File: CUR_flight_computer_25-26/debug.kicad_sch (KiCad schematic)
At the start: 0 parts

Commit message: added dubugging
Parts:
- added D6, D7: ESDA5V3SC5, Package_TO_SOT_SMD:SOT-23-5, symbol Power_Protection:ESDA5V3SC5
- added J6: 3220-14-0100-00, Connector_CNC_Tech:CNC_Tech_3220-14-0100-00, symbol Connector:Conn_ST_STDC14
- added R39: 150, Resistor_SMD:R_0603_1608Metric, symbol Device:R_Small_US
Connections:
- new net: J6.11 (GNDDetect), R39.1
- new net +3V3: J6.3 (VCC)
- new net GND: D6.2 (A), D7.2 (A), J6.5 (GND), J6.7 (GND), R39.2
- new net JCLK/SWCLK: D6.1 (K), J6.6 (JCLK/SWCLK)
- new net JTDI: D6.5 (K), J6.10 (JTDI/NC)
- new net JTDO/SWO: D6.4 (K), J6.8 (JTDO/SWO)
- new net JTMS/SWDIO: D6.3 (K), J6.4 (JTMS/SWDIO)
- new net VCP_RX: D7.5 (K), J6.13 (VCP_RX)
- new net VCP_TX: D7.1 (K), J6.14 (VCP_TX)
- new net ~{RESET}: D7.3 (K), J6.12 (~{RST})
- no-connect marks 0 -> 2
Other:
- note added: "ESD Protection"
- note added: "Reserved (UM2910 pg 11)"
- note added: "Using STLink to align with airbrakes and not pay $50 for the tag connect"
- note added: "also just 02x07 1.27mm so we can do whatever"
- note added: "for STLINK-V3MINIE"
- note added: "meant to be 100 can replace from SMD sampler book if needed"
- note added: "see UM2910 from the debugger's perspective: T_VCP_RX is output T_VCP_TX is input"

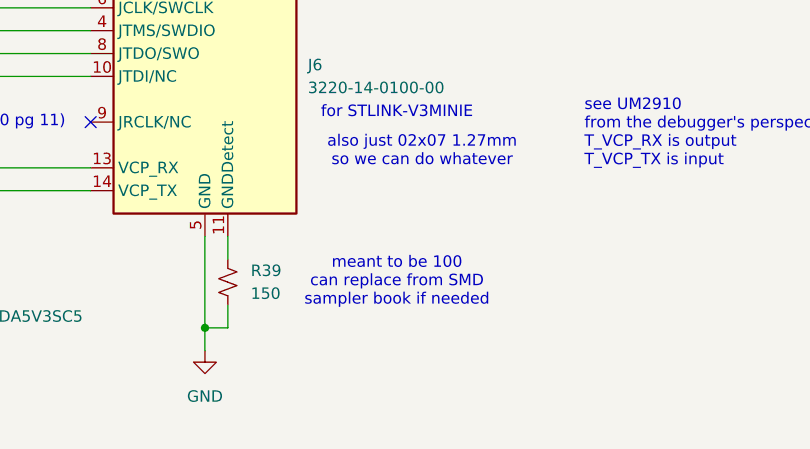
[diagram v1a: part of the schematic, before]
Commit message: changed boot to spdt
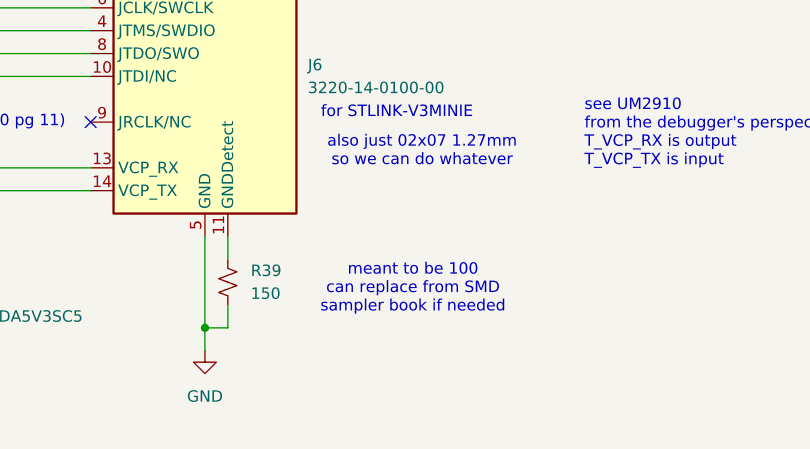
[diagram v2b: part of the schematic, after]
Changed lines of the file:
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@@
 	(text "meant to be 100\ncan replace from SMD\nsampler book if needed"
 		(exclude_from_sim no)
-		(at 134.366 69.85 0)
+		(at 136.144 70.612 0)
 		(effects
 			(font

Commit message: updated all needed fixes
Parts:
- renumbered D6 to D1, D7 to D2, J6 to J1, R39 to R6
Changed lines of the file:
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@@
 		(dnp no)
 		(fields_autoplaced yes)
-		(property "Reference" "J6"
+		(property "Reference" "J1"
 			(at 124.46 45.7199 0)
 			(effects
@@
 			(project "CUR_flight_computer_25-26"
 				(path "/bf7761cc-1b32-4d86-809c-5f027005229b/0389a778-0ae1-4921-8e0e-3c33d2286cb8"
-					(reference "J6")
+					(reference "J1")
 					(unit 1)
 				)
@@
 		(dnp no)
 		(fields_autoplaced yes)
-		(property "Reference" "R39"
+		(property "Reference" "R6"
 			(at 118.11 68.5799 0)
 			(effects
@@
 			(project "CUR_flight_computer_25-26"
 				(path "/bf7761cc-1b32-4d86-809c-5f027005229b/0389a778-0ae1-4921-8e0e-3c33d2286cb8"
-					(reference "R39")
+					(reference "R6")
 					(unit 1)
 				)
@@
 		(dnp no)
 		(fields_autoplaced yes)
-		(property "Reference" "#PWR078"
+		(property "Reference" "#PWR043"
 			(at 113.03 83.82 0)
 			(effects
@@
 			(project "CUR_flight_computer_25-26"
 				(path "/bf7761cc-1b32-4d86-809c-5f027005229b/0389a778-0ae1-4921-8e0e-3c33d2286cb8"
-					(reference "#PWR078")
+					(reference "#PWR043")
 					(unit 1)
 				)
@@
 		(on_board yes)
 		(dnp no)
-		(property "Reference" "D6"
+		(property "Reference" "D1"
 			(at 62.23 71.12 0)
 			(effects
@@
 			(project "CUR_flight_computer_25-26"
 				(path "/bf7761cc-1b32-4d86-809c-5f027005229b/0389a778-0ae1-4921-8e0e-3c33d2286cb8"
-					(reference "D6")
+					(reference "D1")
 					(unit 1)
 				)
@@
 		(dnp no)
 		(fields_autoplaced yes)
-		(property "Reference" "#PWR073"
+		(property "Reference" "#PWR040"
 			(at 54.61 86.36 0)
 			(effects
@@
 			(project "CUR_flight_computer_25-26"
 				(path "/bf7761cc-1b32-4d86-809c-5f027005229b/0389a778-0ae1-4921-8e0e-3c33d2286cb8"
-					(reference "#PWR073")
+					(reference "#PWR040")
 					(unit 1)
 				)
@@
 		(on_board yes)
 		(dnp no)
-		(property "Reference" "D7"
+		(property "Reference" "D2"
 			(at 87.884 71.12 0)
 			(effects
@@
 			(project "CUR_flight_computer_25-26"
 				(path "/bf7761cc-1b32-4d86-809c-5f027005229b/0389a778-0ae1-4921-8e0e-3c33d2286cb8"
-					(reference "D7")
+					(reference "D2")
 					(unit 1)
 				)
@@
 		(dnp no)
 		(fields_autoplaced yes)
-		(property "Reference" "#PWR077"
+		(property "Reference" "#PWR042"
 			(at 113.03 30.48 0)
 			(effects
@@
 			(project "CUR_flight_computer_25-26"
 				(path "/bf7761cc-1b32-4d86-809c-5f027005229b/0389a778-0ae1-4921-8e0e-3c33d2286cb8"
-					(reference "#PWR077")
+					(reference "#PWR042")
 					(unit 1)
 				)
@@
 		(dnp no)
 		(fields_autoplaced yes)
-		(property "Reference" "#PWR074"
+		(property "Reference" "#PWR041"
 			(at 80.01 86.36 0)
 			(effects
@@
 			(project "CUR_flight_computer_25-26"
 				(path "/bf7761cc-1b32-4d86-809c-5f027005229b/0389a778-0ae1-4921-8e0e-3c33d2286cb8"
-					(reference "#PWR074")
-					(unit 1)
-				)
+					(reference "#PWR041")
+					(unit 1)
+				)

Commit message: ahhhh my eyes (decent layout)
put things on both sides
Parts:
- J1: footprint Connector_CNC_Tech:CNC_Tech_3220-14-0100-00 -> Connector_CNC_Tech:CNC_Tech_3020-14-0300-00_CNC
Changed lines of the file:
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@@
 			)
 		)
-		(property "Footprint" "Connector_CNC_Tech:CNC_Tech_3220-14-0100-00"
+		(property "Footprint" "Connector_CNC_Tech:CNC_Tech_3020-14-0300-00_CNC"
 			(at 113.03 46.99 0)
 			(effects

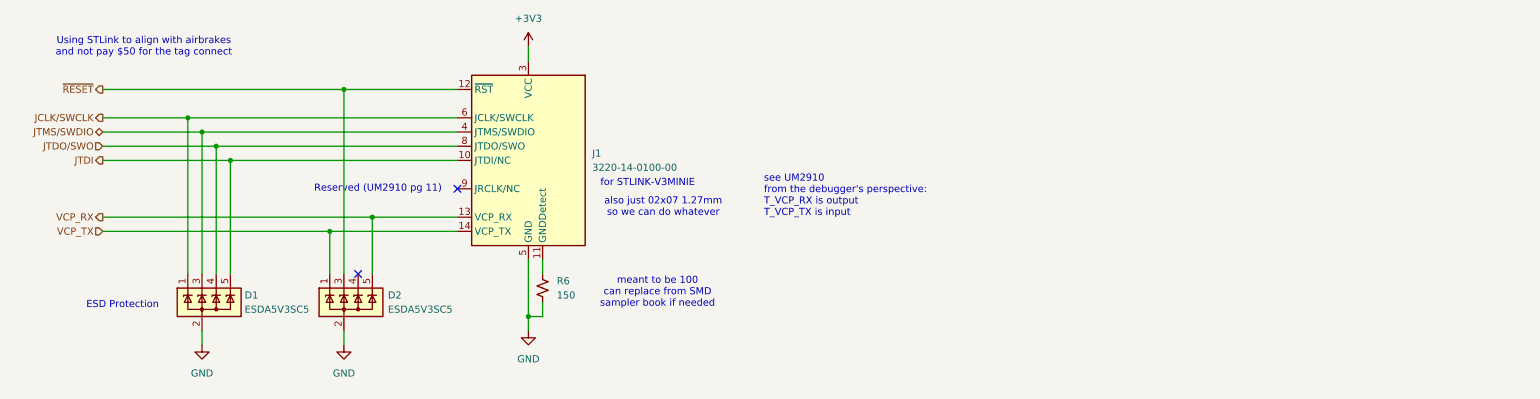
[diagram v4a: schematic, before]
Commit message: added in debug header to layout
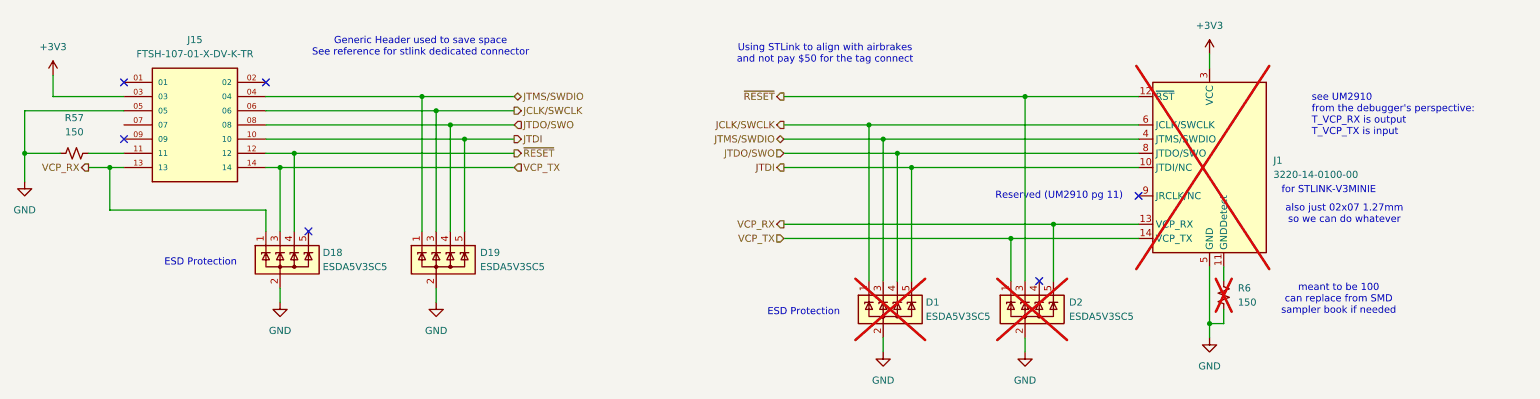
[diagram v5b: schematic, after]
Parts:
- added D18, D19: ESDA5V3SC5, Package_TO_SOT_SMD:SOT-23-5, symbol Power_Protection:ESDA5V3SC5
- added J15: FTSH-107-01-X-DV-K-TR, Connector_SAMTEC_FTSH-107-01-X-DV-K-TR:SAMTEC_FTSH-107-01-X-DV-K-TR, symbol Samtec_FTSH-107-01-X-DV-K-TR:FTSH-107-01-X-DV-K-TR
- added R57: 150, Resistor_SMD:R_0603_1608Metric, symbol Device:R_Small_US
- D1, D2, R6: now not fitted; now left out of the parts list
- J1: footprint Connector_CNC_Tech:CNC_Tech_3020-14-0300-00_CNC -> Connector_SAMTEC_FTSH-107-01-X-DV-K-TR:SAMTEC_FTSH-107-01-X-DV-K-TR; now not fitted; now left out of the parts list
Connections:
- net +3V3: now also J15.03
- net GND: now also D18.2 (A), D19.2 (A), J15.05, R57.1
- net JCLK/SWCLK: now also D19.3 (K), J15.06
- net JTDI: now also D19.5 (K), J15.10
- net JTDO/SWO: now also D19.4 (K), J15.08
- net JTMS/SWDIO: now also D19.1 (K), J15.04
- net VCP_RX: now also D18.1 (K), J15.13
- net VCP_TX: now also D18.3 (K), J15.14
- net ~{RESET}: now also D18.4 (K), J15.12
- new net: J15.11, R57.2
- no-connect marks 2 -> 6
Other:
- note added: "Generic Header used to save space See reference for stlink dedicated connector"

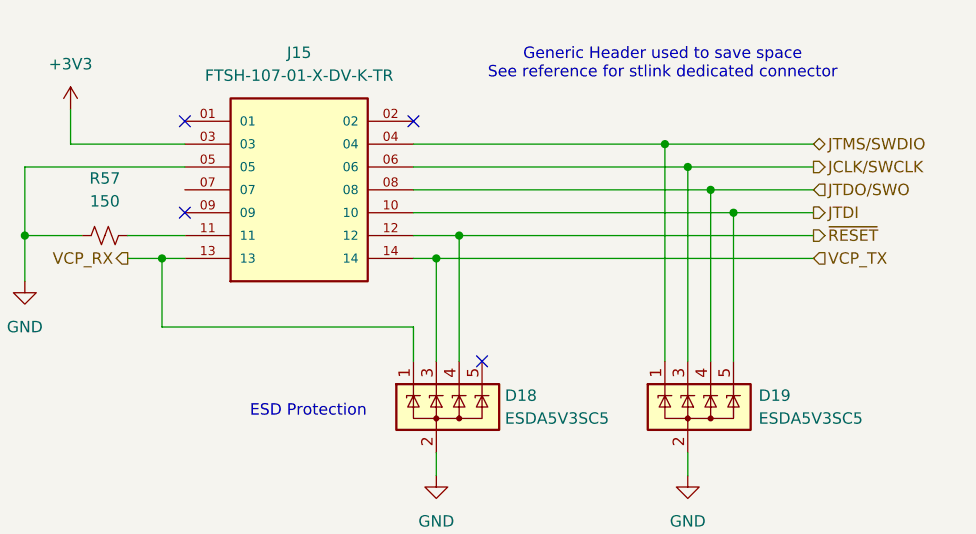
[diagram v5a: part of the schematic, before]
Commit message: started routing power and rf section
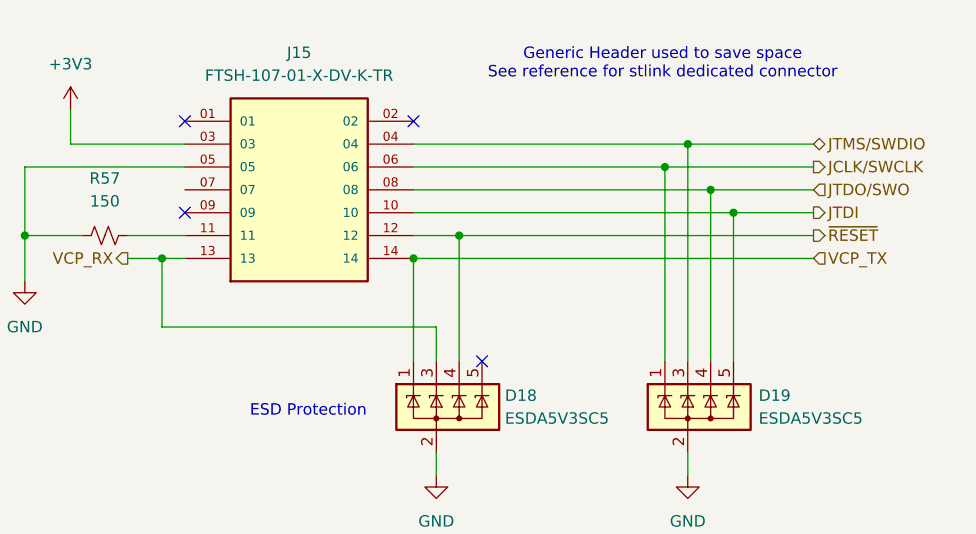
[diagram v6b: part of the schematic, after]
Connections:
- net JCLK/SWCLK: now also D19.1 (K); no longer D19.3 (K)
- net JTMS/SWDIO: now also D19.3 (K); no longer D19.1 (K)
- net VCP_RX: now also D18.3 (K); no longer D18.1 (K)
- net VCP_TX: now also D18.1 (K); no longer D18.3 (K)
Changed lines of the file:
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@@
 	)
 	(junction
-		(at 93.98 35.56)
-		(diameter 0)
-		(color 0 0 0 0)
-	)
-	(junction
-		(at 68.58 48.26)
+		(at 93.98 38.1)
 		(diameter 0)
 		(color 0 0 0 0)
@@
 	)
 	(junction
-		(at 96.52 38.1)
-		(diameter 0)
-		(color 0 0 0 0)
-	)
-	(junction
 		(at 38.1 48.26)
 		(diameter 0)
@@
 	)
 	(junction
+		(at 66.04 48.26)
+		(diameter 0)
+		(color 0 0 0 0)
+	)
+	(junction
 		(at 22.86 45.72)
 		(diameter 0)
@@
 	(junction
 		(at 101.6 43.18)
+		(diameter 0)
+		(color 0 0 0 0)
+	)
+	(junction
+		(at 96.52 35.56)
 		(diameter 0)
 		(color 0 0 0 0)
@@
 	(wire
 		(pts
+			(xy 66.04 35.56) (xy 96.52 35.56)
+		)
+		(stroke
+			(width 0)
+			(type default)
+		)
+	)
+	(wire
+		(pts
+			(xy 66.04 59.69) (xy 66.04 48.26)
+		)
+		(stroke
+			(width 0)
+			(type default)
+		)
+	)
+	(wire
+		(pts
 			(xy 99.06 40.64) (xy 110.49 40.64)
 		)
@@
 	(wire
 		(pts
-			(xy 93.98 35.56) (xy 93.98 59.69)
-		)
-		(stroke
-			(width 0)
-			(type default)
-		)
-	)
-	(wire
-		(pts
 			(xy 66.04 43.18) (xy 101.6 43.18)
 		)
@@
 	(wire
 		(pts
+			(xy 68.58 55.88) (xy 68.58 59.69)
+		)
+		(stroke
+			(width 0)
+			(type default)
+		)
+	)
+	(wire
+		(pts
 			(xy 71.12 45.72) (xy 110.49 45.72)
 		)
@@
 	(wire
 		(pts
-			(xy 96.52 38.1) (xy 110.49 38.1)
+			(xy 93.98 38.1) (xy 110.49 38.1)
+		)
+		(stroke
+			(width 0)
+			(type default)
+		)
+	)
+	(wire
+		(pts
+			(xy 66.04 38.1) (xy 93.98 38.1)
 		)
 		(stroke
@@
 	(wire
 		(pts
-			(xy 66.04 59.69) (xy 66.04 55.88)
-		)
-		(stroke
-			(width 0)
-			(type default)
-		)
-	)
-	(wire
-		(pts
 			(xy 158.75 35.56) (xy 201.93 35.56)
 		)
@@
 	(wire
 		(pts
-			(xy 68.58 48.26) (xy 110.49 48.26)
+			(xy 66.04 48.26) (xy 110.49 48.26)
 		)
 		(stroke
@@
 	(wire
 		(pts
-			(xy 66.04 55.88) (xy 38.1 55.88)
+			(xy 38.1 55.88) (xy 68.58 55.88)
+		)
+		(stroke
+			(width 0)
+			(type default)
+		)
+	)
+	(wire
+		(pts
+			(xy 93.98 38.1) (xy 93.98 59.69)
 		)
 		(stroke
@@
 	(wire
 		(pts
-			(xy 68.58 48.26) (xy 68.58 59.69)
-		)
-		(stroke
-			(width 0)
-			(type default)
-		)
-	)
-	(wire
-		(pts
 			(xy 158.75 43.18) (xy 176.53 43.18)
 		)
@@
 	(wire
 		(pts
+			(xy 96.52 35.56) (xy 110.49 35.56)
+		)
+		(stroke
+			(width 0)
+			(type default)
+		)
+	)
+	(wire
+		(pts
 			(xy 201.93 35.56) (xy 222.25 35.56)
 		)
@@
 	(wire
 		(pts
-			(xy 66.04 38.1) (xy 96.52 38.1)
-		)
-		(stroke
-			(width 0)
-			(type default)
-		)
-	)
-	(wire
-		(pts
 			(xy 101.6 43.18) (xy 101.6 59.69)
 		)
@@
 	(wire
 		(pts
-			(xy 93.98 35.56) (xy 110.49 35.56)
-		)
-		(stroke
-			(width 0)
-			(type default)
-		)
-	)
-	(wire
-		(pts
 			(xy 237.49 68.58) (xy 237.49 66.04)
 		)
@@
 	(wire
 		(pts
-			(xy 96.52 38.1) (xy 96.52 59.69)
-		)
-		(stroke
-			(width 0)
-			(type default)
-		)
-	)
-	(wire
-		(pts
 			(xy 66.04 45.72) (xy 71.12 45.72)
 		)
@@
 	(wire
 		(pts
+			(xy 96.52 35.56) (xy 96.52 59.69)
+		)
+		(stroke
+			(width 0)
+			(type default)
+		)
+	)
+	(wire
+		(pts
 			(xy 27.94 31.75) (xy 27.94 35.56)
 		)
@@
 	(wire
 		(pts
-			(xy 66.04 35.56) (xy 93.98 35.56)
-		)
-		(stroke
-			(width 0)
-			(type default)
-		)
-	)
-	(wire
-		(pts
 			(xy 176.53 78.74) (xy 176.53 81.28)
 		)
@@
 		)
 		(stroke
-			(width 0)
-			(type default)
-		)
-	)
-	(wire
-		(pts
-			(xy 66.04 48.26) (xy 68.58 48.26)
-		)
-		(stroke

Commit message: Layout groups
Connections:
- net JCLK/SWCLK: now also D19.3 (K); no longer D19.1 (K)
- net JTDI: now also D18.5 (K); no longer D19.5 (K)
- net JTMS/SWDIO: now also D19.1 (K); no longer D19.3 (K)
- net VCP_RX: now also D18.4 (K); no longer D18.3 (K)
- net VCP_TX: now also D18.3 (K); no longer D18.1 (K)
- net ~{RESET}: now also D18.1 (K); no longer D18.4 (K)
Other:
- moved on the sheet: D18

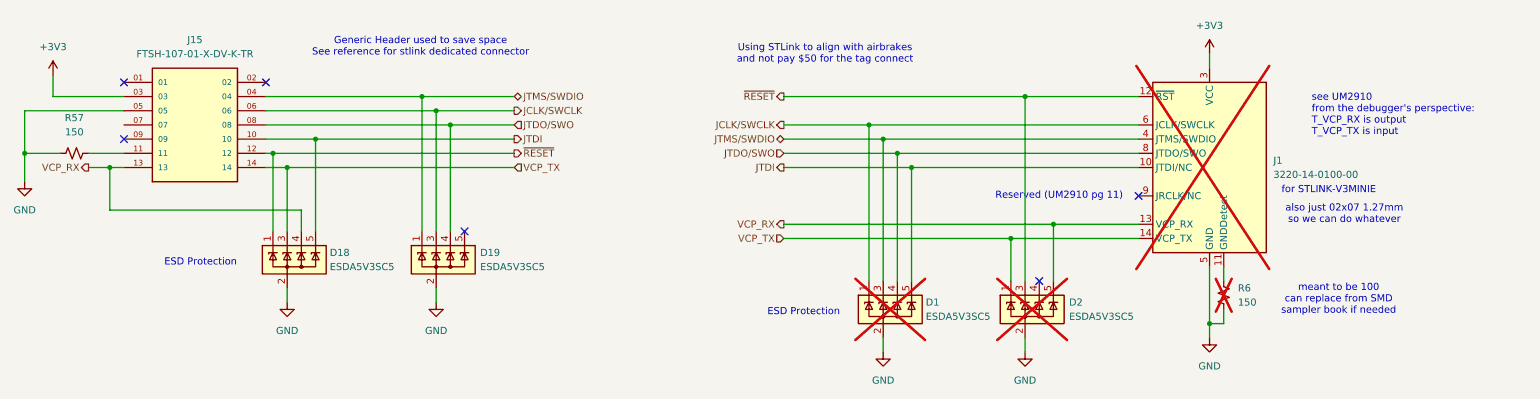
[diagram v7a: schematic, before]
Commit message: Remove JTDI and combine NRST and ~{RESET}
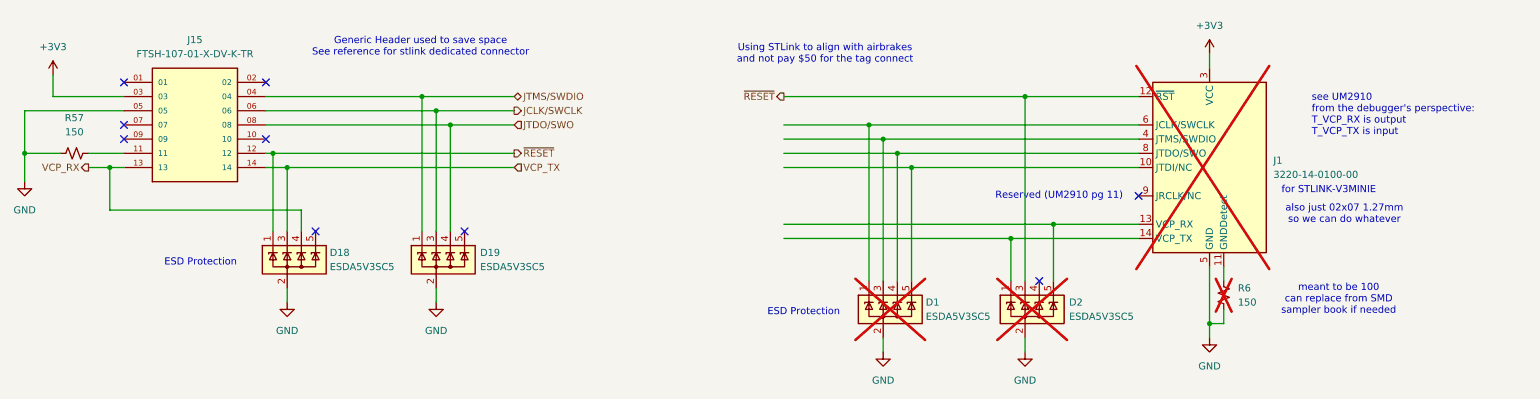
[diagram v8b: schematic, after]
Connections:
- net JCLK/SWCLK: no longer D1.1 (K), J1.6 (JCLK/SWCLK)
- net JTDO/SWO: no longer D1.4 (K), J1.8 (JTDO/SWO)
- net JTMS/SWDIO: no longer D1.3 (K), J1.4 (JTMS/SWDIO)
- net VCP_RX: no longer D2.5 (K), J1.13 (VCP_RX)
- net VCP_TX: no longer D2.1 (K), J1.14 (VCP_TX)
- net JTDI: no longer names the net of D1.5 (K), J1.10 (JTDI/NC)
- net JTDI: no longer D18.5 (K), J15.10
- new net: D2.5 (K), J1.13 (VCP_RX)
- new net: D2.1 (K), J1.14 (VCP_TX)
- new net: D1.3 (K), J1.4 (JTMS/SWDIO)
- new net: D1.1 (K), J1.6 (JCLK/SWCLK)
- new net: D1.4 (K), J1.8 (JTDO/SWO)
- no-connect marks 6 -> 9
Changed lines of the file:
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@@
-	)
-	(junction
-		(at 74.93 43.18)
-		(diameter 0)
-		(color 0 0 0 0)
 	)
 	(junction
@@
 	)
 	(no_connect
+		(at 74.93 59.69)
+	)
+	(no_connect
 		(at 40.64 43.18)
 	)
@@
 	)
 	(no_connect
+		(at 40.64 40.64)
+	)
+	(no_connect
+		(at 66.04 43.18)
+	)
+	(no_connect
 		(at 40.64 33.02)
 	)
@@
 	(wire
 		(pts
-			(xy 66.04 43.18) (xy 74.93 43.18)
-		)
-		(stroke
-			(width 0)
-			(type default)
-		)
-	)
-	(wire
-		(pts
 			(xy 176.53 43.18) (xy 222.25 43.18)
 		)
@@
 	(wire
 		(pts
-			(xy 74.93 43.18) (xy 110.49 43.18)
-		)
-		(stroke
-			(width 0)
-			(type default)
-		)
-	)
-	(wire
-		(pts
-			(xy 74.93 43.18) (xy 74.93 59.69)
-		)
-		(stroke
-			(width 0)
-			(type default)
-		)
-	)
-	(wire
-		(pts
 			(xy 158.75 43.18) (xy 176.53 43.18)
 		)
@@
 			(width 0)
 			(type default)
-		)
-	)
-	(hierarchical_label "VCP_RX"
-		(shape output)
-		(at 158.75 58.42 180)
-		(effects
-			(font
-				(size 1.27 1.27)
-			)
-			(justify right)
 		)
 	)
@@
 	(hierarchical_label "JCLK/SWCLK"
 		(shape output)
-		(at 158.75 40.64 180)
-		(effects
-			(font
-				(size 1.27 1.27)
-			)
-			(justify right)
-		)
-	)
-	(hierarchical_label "JTMS/SWDIO"
-		(shape bidirectional)
-		(at 158.75 43.18 180)
-		(effects
-			(font
-				(size 1.27 1.27)
-			)
-			(justify right)
-		)
-	)
-	(hierarchical_label "JTDO/SWO"
-		(shape input)
-		(at 158.75 45.72 180)
-		(effects
-			(font
-				(size 1.27 1.27)
-			)
-			(justify right)
-		)
-	)
-	(hierarchical_label "JCLK/SWCLK"
-		(shape output)
 		(at 110.49 38.1 0)
 		(effects
@@
 			)
 			(justify left)
-		)
-	)
-	(hierarchical_label "VCP_TX"
-		(shape input)
-		(at 158.75 60.96 180)
-		(effects
-			(font
-				(size 1.27 1.27)
-			)
-			(justify right)
 		)
 	)
@@
 		(effects
 			(font
-				(size 1.27 1.27)
-			)
-			(justify right)
-		)
-	)
-	(hierarchical_label "JTDI"
-		(shape output)
-		(at 110.49 43.18 0)
-		(effects
-			(font
-				(size 1.27 1.27)
-			)
-			(justify left)
-		)
-	)
-	(hierarchical_label "JTDI"
-		(shape output)
-		(at 158.75 48.26 180)
-		(effects
-			(font
